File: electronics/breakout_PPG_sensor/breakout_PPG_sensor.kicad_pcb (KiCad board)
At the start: 2 copper layers, 18.5 x 10.9 mm, 6 parts, among them J1 Conn_01x04, J2 Conn_01x04

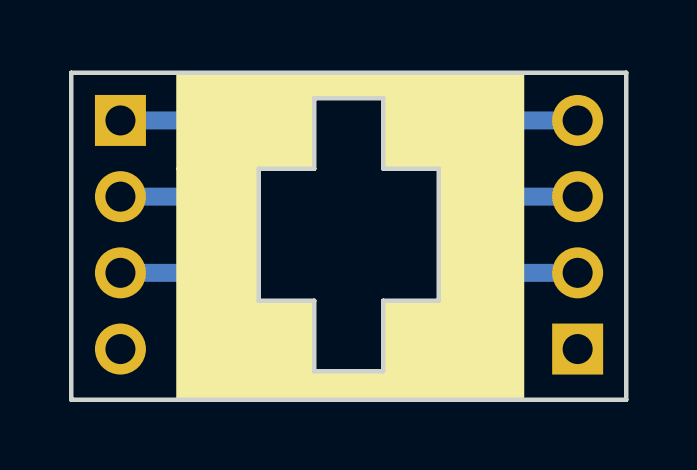
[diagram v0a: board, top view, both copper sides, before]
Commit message: updated breakout for the PPG sensor to new footprint and adjusted cutouts
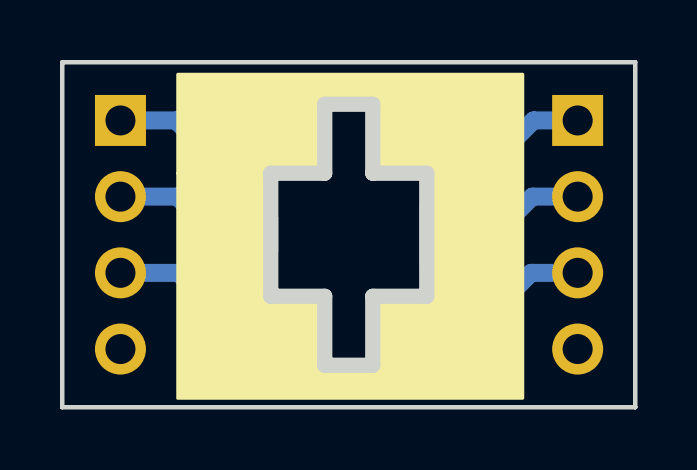
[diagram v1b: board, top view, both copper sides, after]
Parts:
- removed D1, D2: LED, SquantorDiodes:KPTR-3216
- removed D3: D_Photo, SquantorDiodes:SFH2440_reverse
- added U1: PPG_sensor, SquantorOpto:PPG_sensor_reverse, F.Cu at (162.6, 101.6)
- N2: value 20190711 -> 20200709
- moved J2 7.62 mm to (170.2, 97.8), turned to 180 degrees
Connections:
- J1 pad 1: /LED1_A -> /LED2_A
- J1 pad 3: /LED2_A -> /LED1_A
- J2 pad 1: /VSS -> /LED2_C
- J2 pad 2: /LED2_C -> /PD_C
- J2 pad 3: /PD_C -> /LED1_C
- J2 pad 4: /LED1_C -> /VSS
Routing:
- net /LED1_C: track 5.89 -> 6.59 mm
- net /LED1_A: track 5.89 -> 6.57 mm
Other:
- board size 18.5 x 10.9 mm -> 19.1 x 11.5 mm
